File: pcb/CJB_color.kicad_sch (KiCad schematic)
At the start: 24 parts

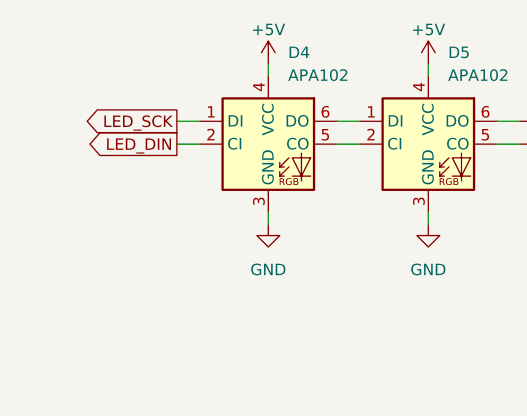
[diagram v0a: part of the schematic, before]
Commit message: Rename apa102 spi clk/data pins
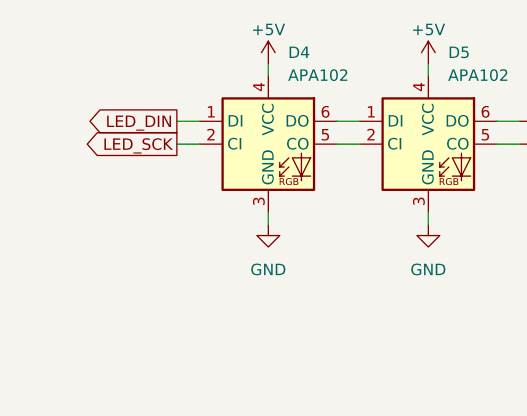
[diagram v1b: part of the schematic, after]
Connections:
- net LED_DIN: now also D4.1 (DI); no longer D4.2 (CI)
- net LED_SCK: now also D4.2 (CI); no longer D4.1 (DI)
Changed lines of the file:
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@@
     (stroke (width 0) (type default))
   )
-  (global_label "LED_DIN" (shape output) (at 40.64 102.87 180) (fields_autoplaced)
+  (global_label "LED_DIN" (shape output) (at 40.64 100.33 180) (fields_autoplaced)
     (effects (font (size 1.27 1.27)) (justify right))
-    (property "Intersheetrefs" "${INTERSHEET_REFS}" (at 30.0348 102.87 0)
+    (property "Intersheetrefs" "${INTERSHEET_REFS}" (at 30.0348 100.33 0)
       (effects (font (size 1.27 1.27)) (justify right) hide)
     )
   )
-  (global_label "LED_SCK" (shape output) (at 40.64 100.33 180) (fields_autoplaced)
+  (global_label "LED_SCK" (shape output) (at 40.64 102.87 180) (fields_autoplaced)
     (effects (font (size 1.27 1.27)) (justify right))
-    (property "Intersheetrefs" "${INTERSHEET_REFS}" (at 29.4906 100.33 0)
+    (property "Intersheetrefs" "${INTERSHEET_REFS}" (at 29.4906 102.87 0)
       (effects (font (size 1.27 1.27)) (justify right) hide)
     )
